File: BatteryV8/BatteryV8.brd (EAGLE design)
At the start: 85 x 85 mm, 69 parts, among them IC1 MAX6462XR29T, Q1 MOSFET-PCHANNEL, Q2 MOSFET-PCHANNEL, Q3 MOSFET-PCHANNEL, X1 MINI-USB-UX60-MB-5ST

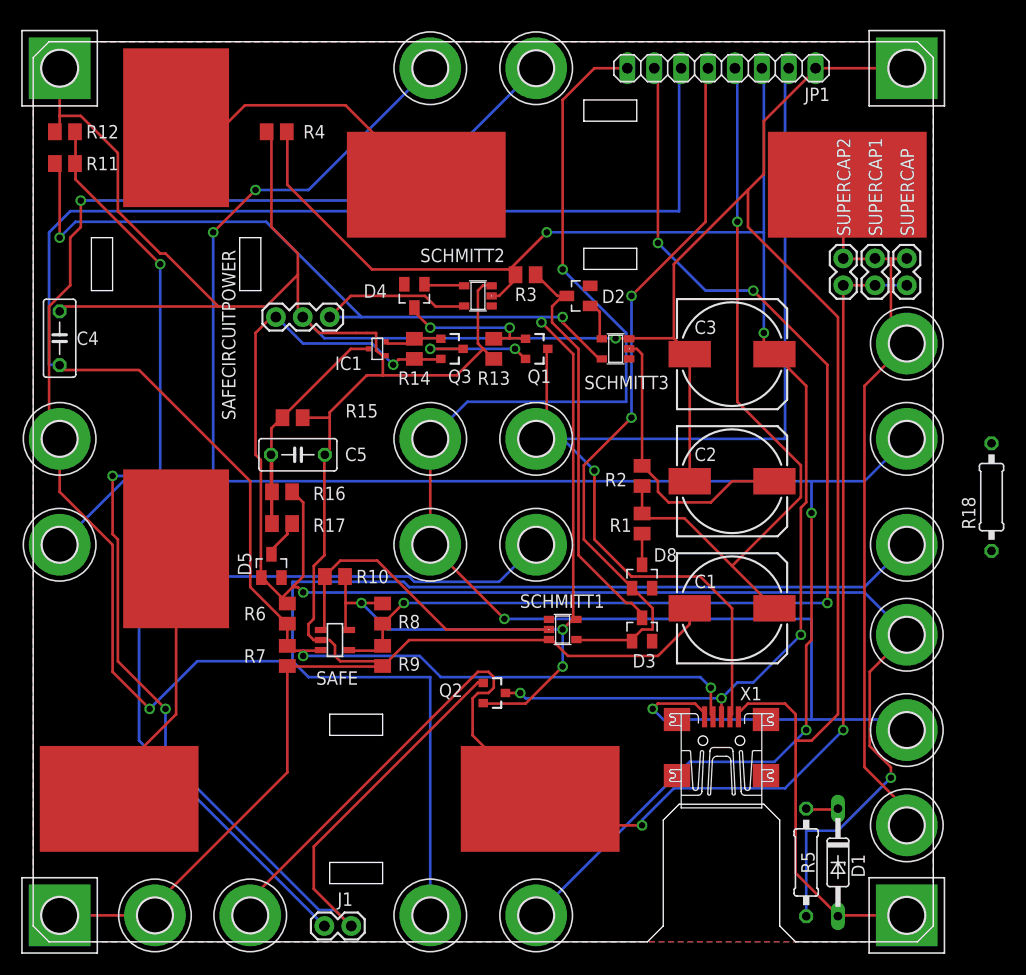
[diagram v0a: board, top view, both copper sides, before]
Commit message: updated schematics and BOM with notes in the course of assembling the 3 main PCBs
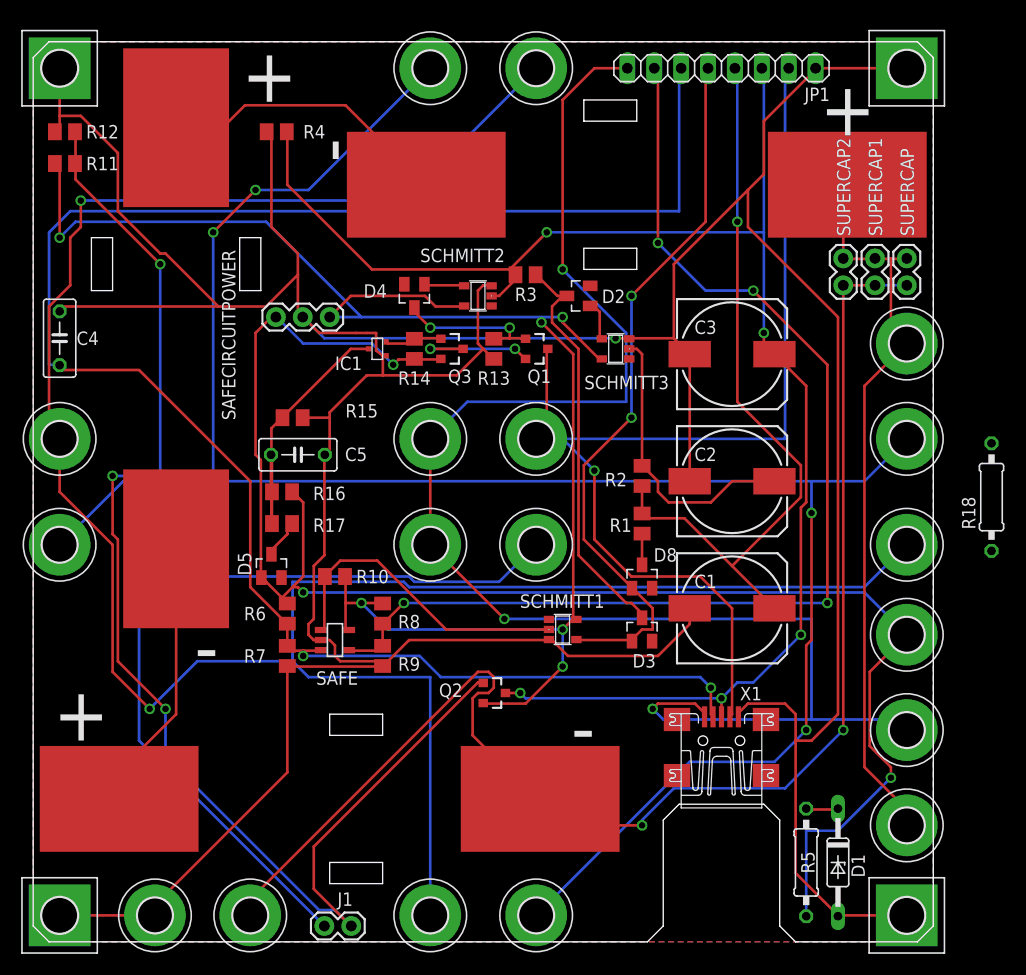
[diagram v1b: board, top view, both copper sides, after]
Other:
- board text added: "+"
- board text added: "-"
- board text added: "Pololu 5V"
- board text removed: "Pololu 3.3v"
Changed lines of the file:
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@@
 <layer number="14" name="Route14" color="22" fill="1" visible="no" active="yes"/>
 <layer number="15" name="Route15" color="23" fill="1" visible="no" active="yes"/>
-<layer number="16" name="Bottom" color="1" fill="1" visible="no" active="yes"/>
+<layer number="16" name="Bottom" color="1" fill="1" visible="yes" active="yes"/>
 <layer number="17" name="Pads" color="2" fill="1" visible="yes" active="yes"/>
 <layer number="18" name="Vias" color="2" fill="1" visible="yes" active="yes"/>
@@
 <layer number="20" name="Dimension" color="15" fill="1" visible="yes" active="yes"/>
 <layer number="21" name="tPlace" color="7" fill="1" visible="yes" active="yes"/>
-<layer number="22" name="bPlace" color="7" fill="1" visible="no" active="yes"/>
-<layer number="23" name="tOrigins" color="15" fill="1" visible="yes" active="yes"/>
+<layer number="22" name="bPlace" color="7" fill="1" visible="yes" active="yes"/>
+<layer number="23" name="tOrigins" color="15" fill="1" visible="no" active="yes"/>
 <layer number="24" name="bOrigins" color="15" fill="1" visible="no" active="yes"/>
-<layer number="25" name="tNames" color="7" fill="1" visible="yes" active="yes"/>
-<layer number="26" name="bNames" color="7" fill="1" visible="no" active="yes"/>
+<layer number="25" name="tNames" color="7" fill="1" visible="no" active="yes"/>
+<layer number="26" name="bNames" color="7" fill="1" visible="yes" active="yes"/>
 <layer number="27" name="tValues" color="7" fill="1" visible="no" active="yes"/>
 <layer number="28" name="bValues" color="7" fill="1" visible="no" active="yes"/>
@@
 <layer number="37" name="tTest" color="7" fill="1" visible="no" active="yes"/>
 <layer number="38" name="bTest" color="7" fill="1" visible="no" active="yes"/>
-<layer number="39" name="tKeepout" color="4" fill="11" visible="yes" active="yes"/>
+<layer number="39" name="tKeepout" color="4" fill="11" visible="no" active="yes"/>
 <layer number="40" name="bKeepout" color="1" fill="11" visible="no" active="yes"/>
-<layer number="41" name="tRestrict" color="4" fill="10" visible="yes" active="yes"/>
+<layer number="41" name="tRestrict" color="4" fill="10" visible="no" active="yes"/>
 <layer number="42" name="bRestrict" color="1" fill="10" visible="no" active="yes"/>
 <layer number="43" name="vRestrict" color="2" fill="10" visible="no" active="yes"/>
@@
 <wire x1="29.5" y1="45.5" x2="29.5" y2="58" width="0.1524" layer="22"/>
 <wire x1="29.5" y1="58" x2="20" y2="58" width="0.1524" layer="22"/>
-<text x="29" y="47" size="1.27" layer="22" rot="MR0">Pololu 3.3v</text>
+<text x="29" y="47" size="1.27" layer="22" rot="MR0">Pololu 5V</text>
+<text x="50.8" y="15.24" size="5.08" layer="21" font="vector">-</text>
+<text x="15.24" y="22.86" size="5.08" layer="21" font="vector">-</text>
+<text x="30.48" y="71.12" size="5.08" layer="21" font="vector" rot="R90">-</text>
+<text x="1.905" y="16.51" size="5.08" layer="21" font="vector">+</text>
+<text x="19.685" y="76.835" size="5.08" layer="21" font="vector">+</text>
+<text x="74.295" y="73.66" size="5.08" layer="21" font="vector">+</text>
 </plain>
 <attributes>

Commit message: Modified schematic and BOM to represent actual board - Smitt triggers. Extracted library elements from schematic and created two local libraries with all the non standard or modified elements used on the board. Circuit analysis and write up of functional spec.
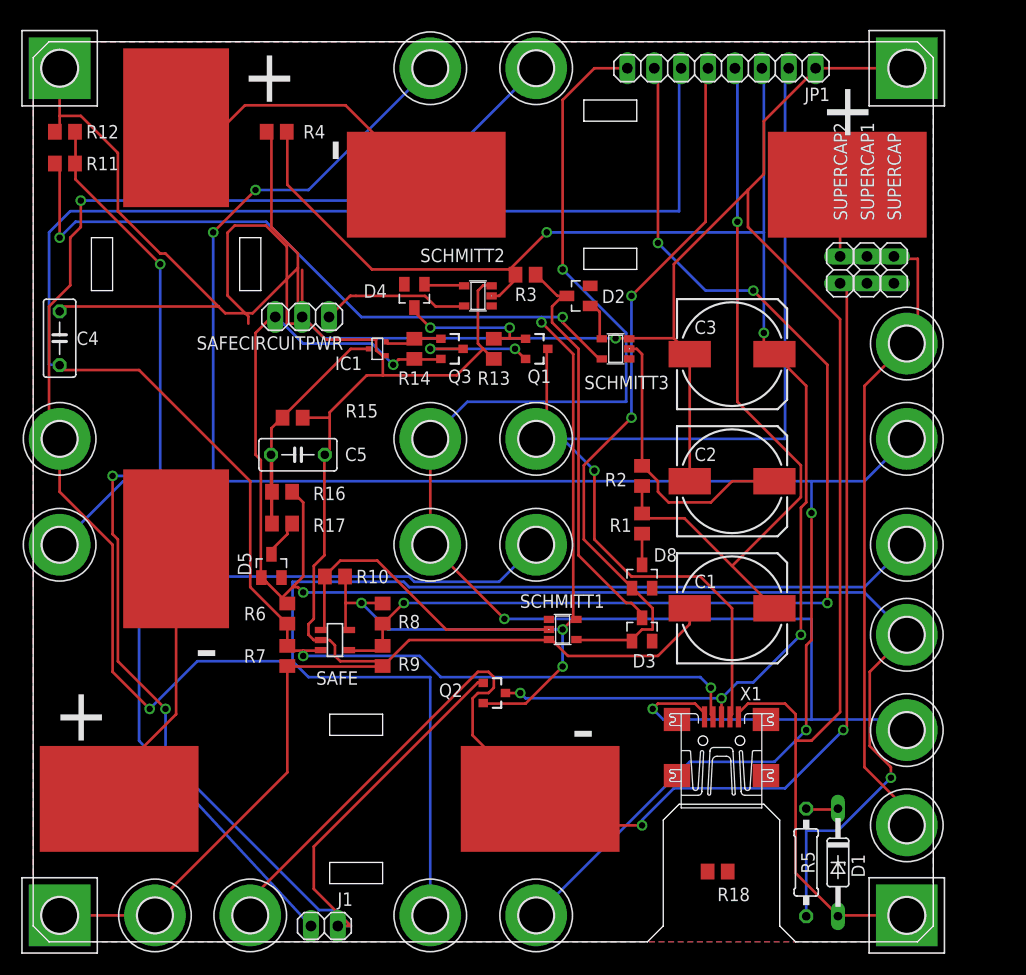
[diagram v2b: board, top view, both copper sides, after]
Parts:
- removed SAFECIRCUITPOWER: Pololu 5V, S10V4F5, SparkFun-Connectors:1X03
- added SAFECIRCUITPWR: (no value), pinhead:1X03
- C1, C2, C3: device adafruit:153CLV-1010 -> rcl:153CLV-1010
- H13, H14, H15, H16, H17, H18, H19, H20, H21, H22: value (none) -> MOUNT-PAD-ROUND3.3
- IC1: device EdgeCube:SC70-3 -> BatteryV8:EDGECUBE_SC70-3
- J1, SUPERCAP, SUPERCAP1, SUPERCAP2: device SparkFun-Connectors:1X02 -> pinhead:1X02
- Q1, Q2, Q3: value MOSFET-PCHANNEL -> MOSFET P-CH
- R1, R10, R11, R12, R13, R14, R15, R16, R17, R2, R3, R4, R6, R7, R8, R9: device adafruit:M0805 -> rcl:R0805
- R18: device rcl:0207/10 -> rcl:R0805
- R5: value NP -> 9999
- SCHMITT1: value 74AUC1G14DBV -> SN74LVC1G14DBVR
- SCHMITT2, SCHMITT3: value 74AUC1G14DBV -> 74LVC1G17DBV
- U$5, U$6, U$7: value AA-BATT -> JST-WATCH_AA-BATT; device JST-Watch:AA-BATT -> BatteryV8:JST-WATCH_AA-BATT
- moved R18 43.8 mm to (64.6, 4.14), turned to 180 degrees
- moved SUPERCAP 1.90 mm to (81.3, 61.0)
- moved SUPERCAP1 1.65 mm to (78.7, 61.0)
- moved SUPERCAP2 1.49 mm to (76.2, 61.0)
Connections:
- removed net N$22: D5.1, H18.B3,3, Q3.2, R14.1, R16.1, R5.2, R6.1, SAFECIRCUITPOWER.3
- new net V-BATTERY: D5.1, H18.B3,3, Q3.2, R14.1, R16.1, R5.2, R6.1, SAFECIRCUITPWR.3
- net +5V: now also SAFECIRCUITPWR.1; no longer SAFECIRCUITPOWER.1
- net GND: now also SAFECIRCUITPWR.2; no longer SAFECIRCUITPOWER.2
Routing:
- net N$22: track 152.9 -> 0.00 mm, vias 3 -> 0
- net V-BATTERY: track 0.00 -> 152.8 mm, vias 0 -> 3
- net GND: track 409.1 -> 438.7 mm
- net +5V: track 154.8 -> 151.9 mm
- net SHDN: track 124.6 -> 127.0 mm
- net N$19: track 71.8 -> 72.7 mm
- net N$23: track 79.4 -> 78.5 mm
